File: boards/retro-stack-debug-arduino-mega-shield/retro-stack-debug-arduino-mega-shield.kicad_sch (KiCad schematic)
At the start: 9 parts, among them J1 Power, J2 PWM, J3 Analog, J4 PWM, J5 Analog, J6 Communication, J7 Digital, J8 BUS_6502

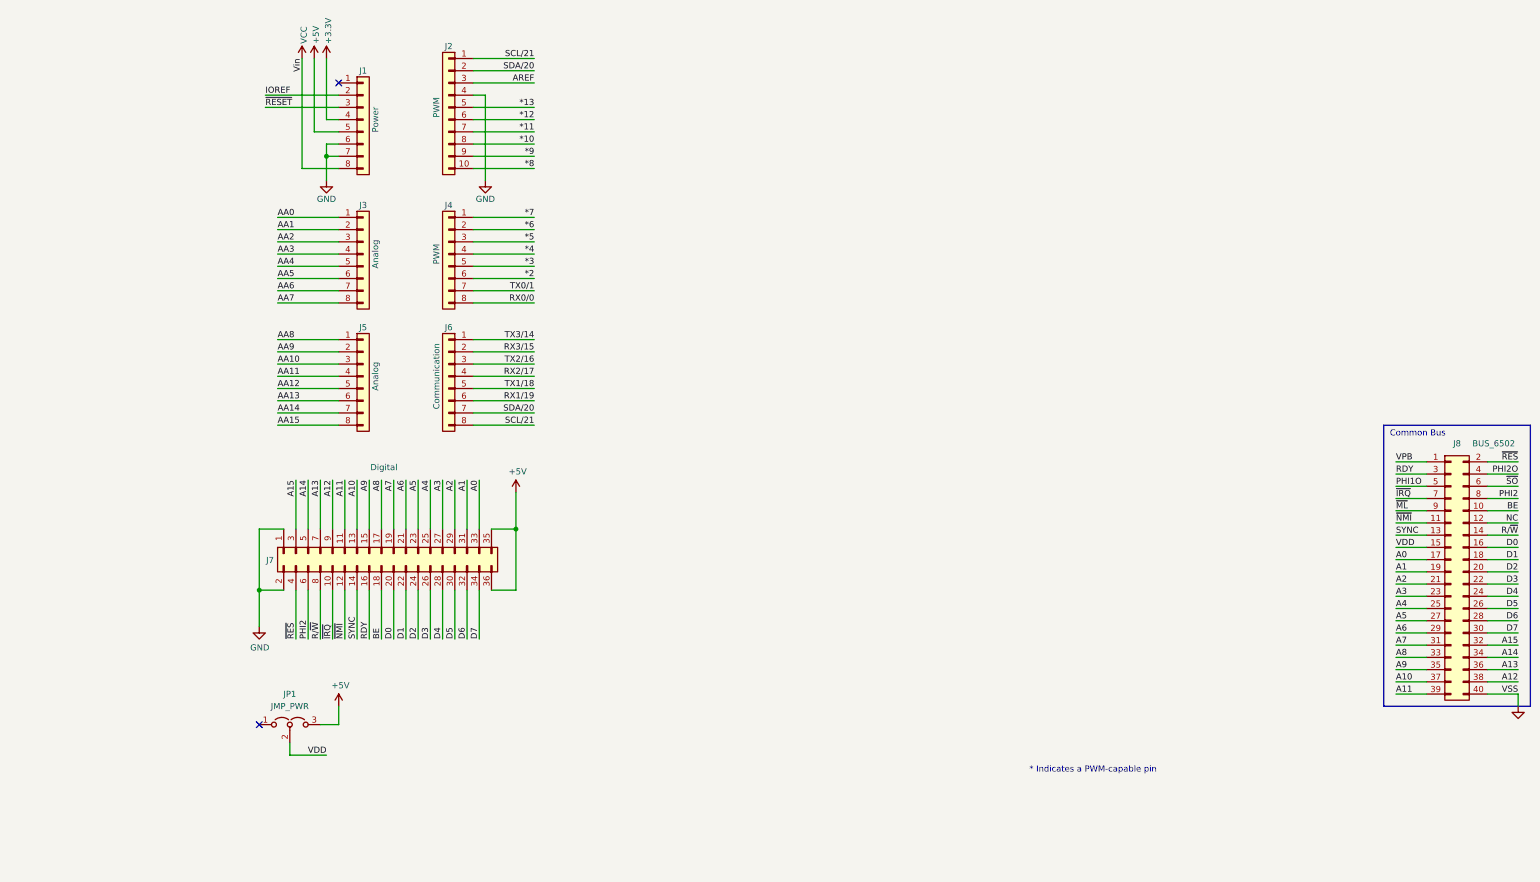
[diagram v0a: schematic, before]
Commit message: Completed rev 0 of cpu, debug, and debug shield boards.
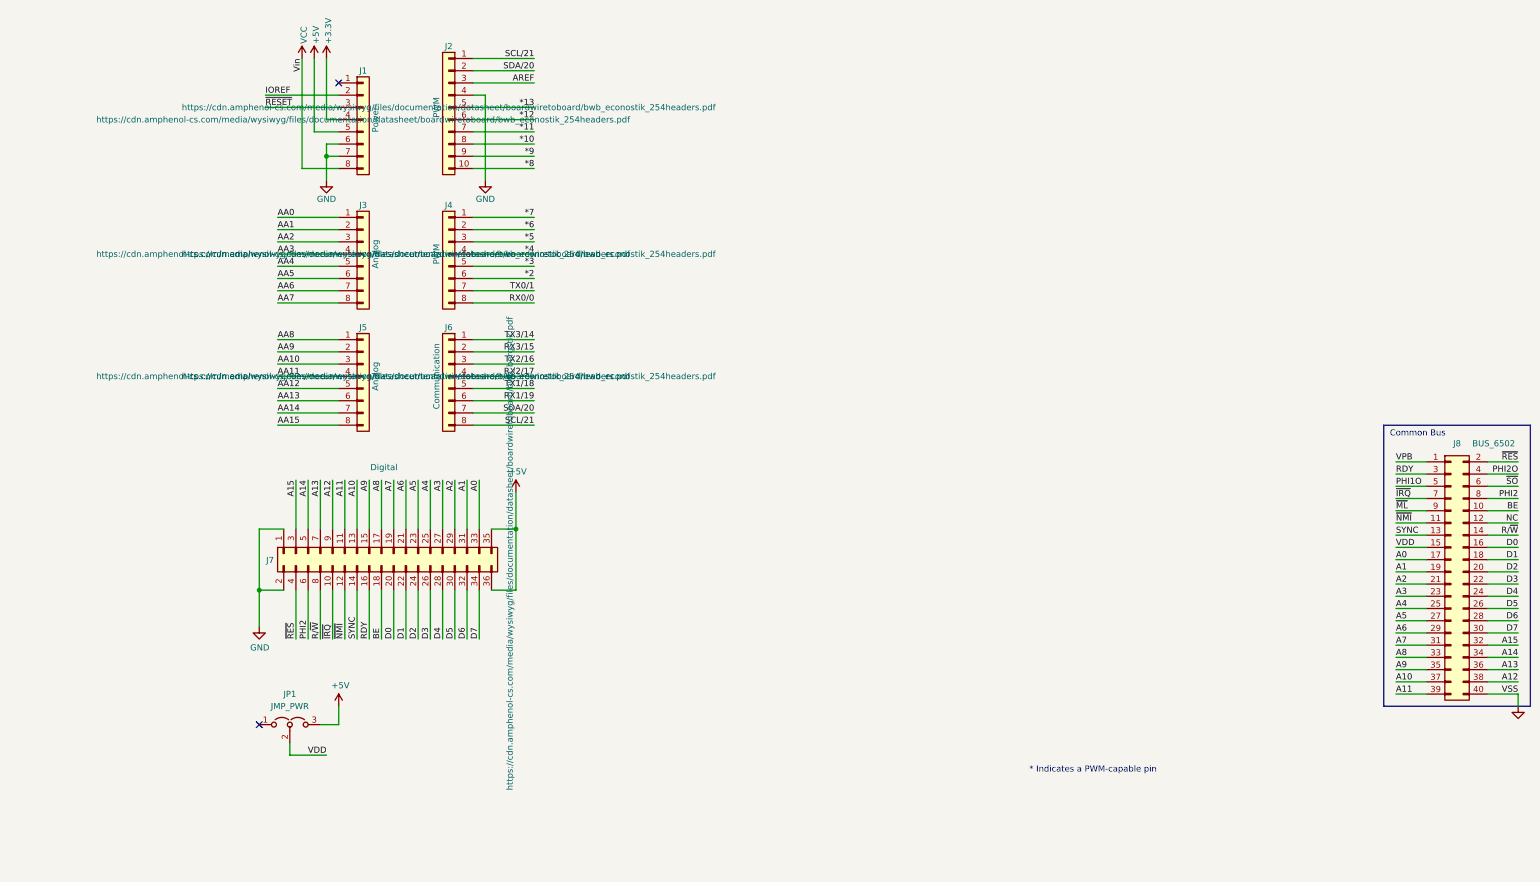
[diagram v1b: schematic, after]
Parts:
- J1, J3, J4, J5, J6: Mfr (none) -> Amphenol; Mfr Part (none) -> 10129378-908001BLF; Supplier (none) -> Mouser; Supplier Part (none) -> 649-1012937890801BLF
- J2: Mfr (none) -> Amphenol; Mfr Part (none) -> 10129378-910001BLF; Supplier (none) -> Mouser; Supplier Part (none) -> 649-1012937891001BLF
- J7: Mfr (none) -> Amphenol; Mfr Part (none) -> 77313-818-36LF; Supplier (none) -> Mouser; Supplier Part (none) -> 649-77313-818-36LF
- J8: Mfr Adafruit -> 3M; Mfr Part 1979 -> 30340-6002HB; Supplier Part 485-1979 -> 517-30340-6002
- JP1: Mfr (none) -> Amphenol; Mfr Part (none) -> 10129378-903001BLF; Supplier (none) -> Mouser; Supplier Part (none) -> 649-1012937890301BLF
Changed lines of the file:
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@@
       (effects (font (size 1.27 1.27)) hide)
     )
-    (property "Datasheet" "" (id 3) (at 39.37 39.37 0))
+    (property "Datasheet" "https://cdn.amphenol-cs.com/media/wysiwyg/files/documentation/datasheet/boardwiretoboard/bwb_econostik_254headers.pdf" (id 3) (at 39.37 39.37 0))
+    (property "Mfr" "Amphenol" (id 4) (at 39.37 39.37 0)
+      (effects (font (size 1.27 1.27)) hide)
+    )
+    (property "Mfr Part" "10129378-908001BLF" (id 5) (at 39.37 39.37 0)
+      (effects (font (size 1.27 1.27)) hide)
+    )
+    (property "Supplier Part" "649-1012937890801BLF" (id 6) (at 39.37 39.37 0)
+      (effects (font (size 1.27 1.27)) hide)
+    )
+    (property "Supplier" "Mouser" (id 7) (at 39.37 39.37 0)
+      (effects (font (size 1.27 1.27)) hide)
+    )
     (pin "1")
     (pin "2")
@@
       (effects (font (size 1.27 1.27)) hide)
     )
-    (property "Datasheet" "" (id 3) (at 57.15 36.83 0))
+    (property "Datasheet" "https://cdn.amphenol-cs.com/media/wysiwyg/files/documentation/datasheet/boardwiretoboard/bwb_econostik_254headers.pdf" (id 3) (at 57.15 36.83 0))
+    (property "Mfr" "Amphenol" (id 4) (at 57.15 36.83 0)
+      (effects (font (size 1.27 1.27)) hide)
+    )
+    (property "Mfr Part" "10129378-910001BLF" (id 5) (at 57.15 36.83 0)
+      (effects (font (size 1.27 1.27)) hide)
+    )
+    (property "Supplier Part" "649-1012937891001BLF" (id 6) (at 57.15 36.83 0)
+      (effects (font (size 1.27 1.27)) hide)
+    )
+    (property "Supplier" "Mouser" (id 7) (at 57.15 36.83 0)
+      (effects (font (size 1.27 1.27)) hide)
+    )
     (pin "1")
     (pin "10")
@@
       (effects (font (size 1.27 1.27)) hide)
     )
-    (property "Datasheet" "" (id 3) (at 39.37 67.31 0))
+    (property "Datasheet" "https://cdn.amphenol-cs.com/media/wysiwyg/files/documentation/datasheet/boardwiretoboard/bwb_econostik_254headers.pdf" (id 3) (at 39.37 67.31 0))
+    (property "Mfr" "Amphenol" (id 4) (at 39.37 67.31 0)
+      (effects (font (size 1.27 1.27)) hide)
+    )
+    (property "Mfr Part" "10129378-908001BLF" (id 5) (at 39.37 67.31 0)
+      (effects (font (size 1.27 1.27)) hide)
+    )
+    (property "Supplier Part" "649-1012937890801BLF" (id 6) (at 39.37 67.31 0)
+      (effects (font (size 1.27 1.27)) hide)
+    )
+    (property "Supplier" "Mouser" (id 7) (at 39.37 67.31 0)
+      (effects (font (size 1.27 1.27)) hide)
+    )
     (pin "1")
     (pin "2")
@@
       (effects (font (size 1.27 1.27)) hide)
     )
-    (property "Datasheet" "" (id 3) (at 57.15 67.31 0))
+    (property "Datasheet" "https://cdn.amphenol-cs.com/media/wysiwyg/files/documentation/datasheet/boardwiretoboard/bwb_econostik_254headers.pdf" (id 3) (at 57.15 67.31 0))
+    (property "Mfr" "Amphenol" (id 4) (at 57.15 67.31 0)
+      (effects (font (size 1.27 1.27)) hide)
+    )
+    (property "Mfr Part" "10129378-908001BLF" (id 5) (at 57.15 67.31 0)
+      (effects (font (size 1.27 1.27)) hide)
+    )
+    (property "Supplier Part" "649-1012937890801BLF" (id 6) (at 57.15 67.31 0)
+      (effects (font (size 1.27 1.27)) hide)
+    )
+    (property "Supplier" "Mouser" (id 7) (at 57.15 67.31 0)
+      (effects (font (size 1.27 1.27)) hide)
+    )
     (pin "1")
     (pin "2")
@@
       (effects (font (size 1.27 1.27)) hide)
     )
-    (property "Datasheet" "" (id 3) (at 39.37 92.71 0))
+    (property "Datasheet" "https://cdn.amphenol-cs.com/media/wysiwyg/files/documentation/datasheet/boardwiretoboard/bwb_econostik_254headers.pdf" (id 3) (at 39.37 92.71 0))
+    (property "Mfr" "Amphenol" (id 4) (at 39.37 92.71 0)
+      (effects (font (size 1.27 1.27)) hide)
+    )
+    (property "Mfr Part" "10129378-908001BLF" (id 5) (at 39.37 92.71 0)
+      (effects (font (size 1.27 1.27)) hide)
+    )
+    (property "Supplier Part" "649-1012937890801BLF" (id 6) (at 39.37 92.71 0)
+      (effects (font (size 1.27 1.27)) hide)
+    )
+    (property "Supplier" "Mouser" (id 7) (at 39.37 92.71 0)
+      (effects (font (size 1.27 1.27)) hide)
+    )
     (pin "1")
     (pin "2")
@@
       (effects (font (size 1.27 1.27)) hide)
     )
-    (property "Datasheet" "" (id 3) (at 57.15 92.71 0))
+    (property "Datasheet" "https://cdn.amphenol-cs.com/media/wysiwyg/files/documentation/datasheet/boardwiretoboard/bwb_econostik_254headers.pdf" (id 3) (at 57.15 92.71 0))
+    (property "Mfr" "Amphenol" (id 4) (at 57.15 92.71 0)
+      (effects (font (size 1.27 1.27)) hide)
+    )
+    (property "Mfr Part" "10129378-908001BLF" (id 5) (at 57.15 92.71 0)
+      (effects (font (size 1.27 1.27)) hide)
+    )
+    (property "Supplier Part" "649-1012937890801BLF" (id 6) (at 57.15 92.71 0)
+      (effects (font (size 1.27 1.27)) hide)
+    )
+    (property "Supplier" "Mouser" (id 7) (at 57.15 92.71 0)
+      (effects (font (size 1.27 1.27)) hide)
+    )
     (pin "1")
     (pin "2")
@@
       (effects (font (size 1.27 1.27)) hide)
     )
-    (property "Datasheet" "" (id 3) (at 69.85 129.54 0))
+    (property "Datasheet" "https://cdn.amphenol-cs.com/media/wysiwyg/files/documentation/datasheet/boardwiretoboard/bwb_bergstik.pdf" (id 3) (at 69.85 129.54 0))
+    (property "Mfr" "Amphenol" (id 4) (at 43.18 129.54 0)
+      (effects (font (size 1.27 1.27)) hide)
+    )
+    (property "Mfr Part" "77313-818-36LF" (id 5) (at 43.18 129.54 0)
+      (effects (font (size 1.27 1.27)) hide)
+    )
+    (property "Supplier Part" "649-77313-818-36LF" (id 6) (at 43.18 129.54 0)
+      (effects (font (size 1.27 1.27)) hide)
+    )
+    (property "Supplier" "Mouser" (id 7) (at 43.18 129.54 0)
+      (effects (font (size 1.27 1.27)) hide)
+    )
     (pin "1")
     (pin "10")
@@
       (effects (font (size 1.27 1.27)) hide)
     )
-    (property "Datasheet" "~" (id 3) (at 24.13 165.1 0)
+    (property "Datasheet" "https://cdn.amphenol-cs.com/media/wysiwyg/files/documentation/datasheet/boardwiretoboard/bwb_econostik_254headers.pdf" (id 3) (at 24.13 165.1 0)
+      (effects (font (size 1.27 1.27)) hide)
+    )
+    (property "Mfr" "Amphenol" (id 4) (at 24.13 165.1 0)
+      (effects (font (size 1.27 1.27)) hide)
+    )
+    (property "Mfr Part" "10129378-903001BLF" (id 5) (at 24.13 165.1 0)
+      (effects (font (size 1.27 1.27)) hide)
+    )
+    (property "Supplier Part" "649-1012937890301BLF" (id 6) (at 24.13 165.1 0)
+      (effects (font (size 1.27 1.27)) hide)
+    )
+    (property "Supplier" "Mouser" (id 7) (at 24.13 165.1 0)
       (effects (font (size 1.27 1.27)) hide)
     )
@@
       (effects (font (size 1.27 1.27)) hide)
     )
-    (property "Datasheet" "https://www.adafruit.com/product/1979#technical-details" (id 3) (at 265.43 133.35 0)
-      (effects (font (size 1.27 1.27)) hide)
-    )
-    (property "Mfr" "Adafruit" (id 4) (at 265.43 133.35 0)
-      (effects (font (size 1.27 1.27)) hide)
-    )
-    (property "Mfr Part" "1979 " (id 5) (at 265.43 133.35 0)
+    (property "Datasheet" "https://www.mouser.com/datasheet/2/1/c315a08499b0d0804b11b538e0036d96398e6fbf-2951615.pdf" (id 3) (at 265.43 133.35 0)
+      (effects (font (size 1.27 1.27)) hide)
+    )
+    (property "Mfr" "3M" (id 4) (at 265.43 133.35 0)
+      (effects (font (size 1.27 1.27)) hide)
+    )
+    (property "Mfr Part" "30340-6002HB" (id 5) (at 265.43 133.35 0)
       (effects (font (size 1.27 1.27)) hide)
     )
@@
       (effects (font (size 1.27 1.27)) hide)
     )
-    (property "Supplier Part" "485-1979" (id 7) (at 265.43 133.35 0)
-      (effects (font (size 1.27 1.27)) hide)
-    )
+    (property "Supplier Part" "517-30340-6002" (id 7) (at 265.43 133.35 0)
+      (effects (font (size 1.27 1.27)) hide)
+    )

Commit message: Update documentation for recently completed board revisions.
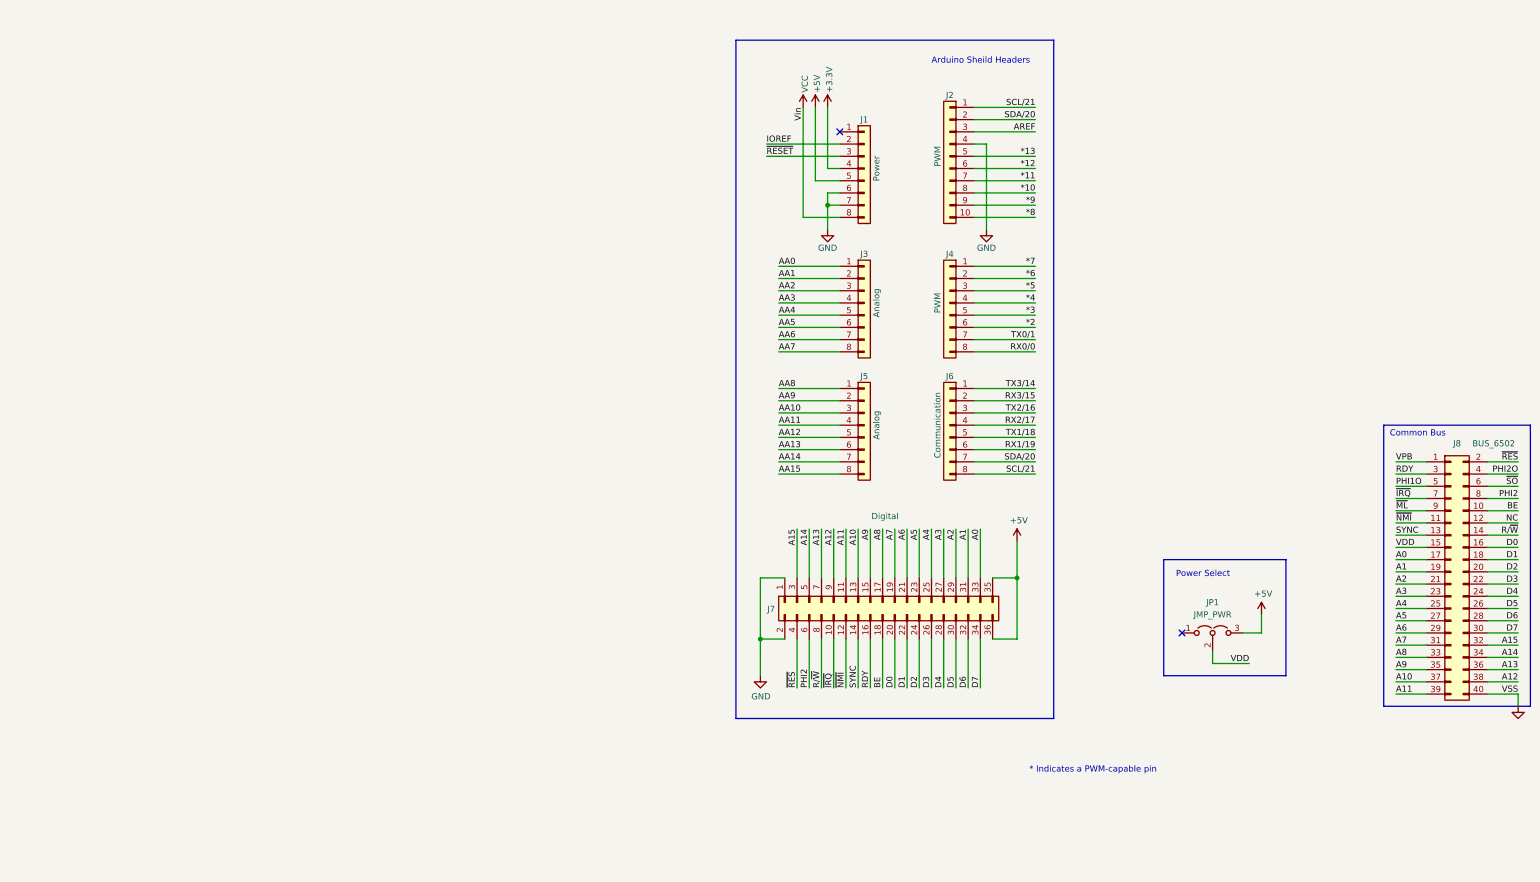
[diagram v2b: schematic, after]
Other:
- note added: "Arduino Sheild Headers"
- note added: "Power Select"
- moved on the sheet: J1, J2, J3, J4, J5, J6, J7, JP1
